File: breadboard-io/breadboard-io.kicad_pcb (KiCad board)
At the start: 2 copper layers, 33 x 19.1 mm, 25 parts, among them J1 Conn_01x10_Male, Q1 DMN3300U, Q2 DMN3300U, Q3 DMN3300U, Q4 DMN3300U, SW1 SW0, SW2 SW0, SW3 SW0, SW4 SW0

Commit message: Committing and ordering Rev-1
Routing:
- net GND: track 1.47 -> 0.00 mm
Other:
- board text added: "rev-1"

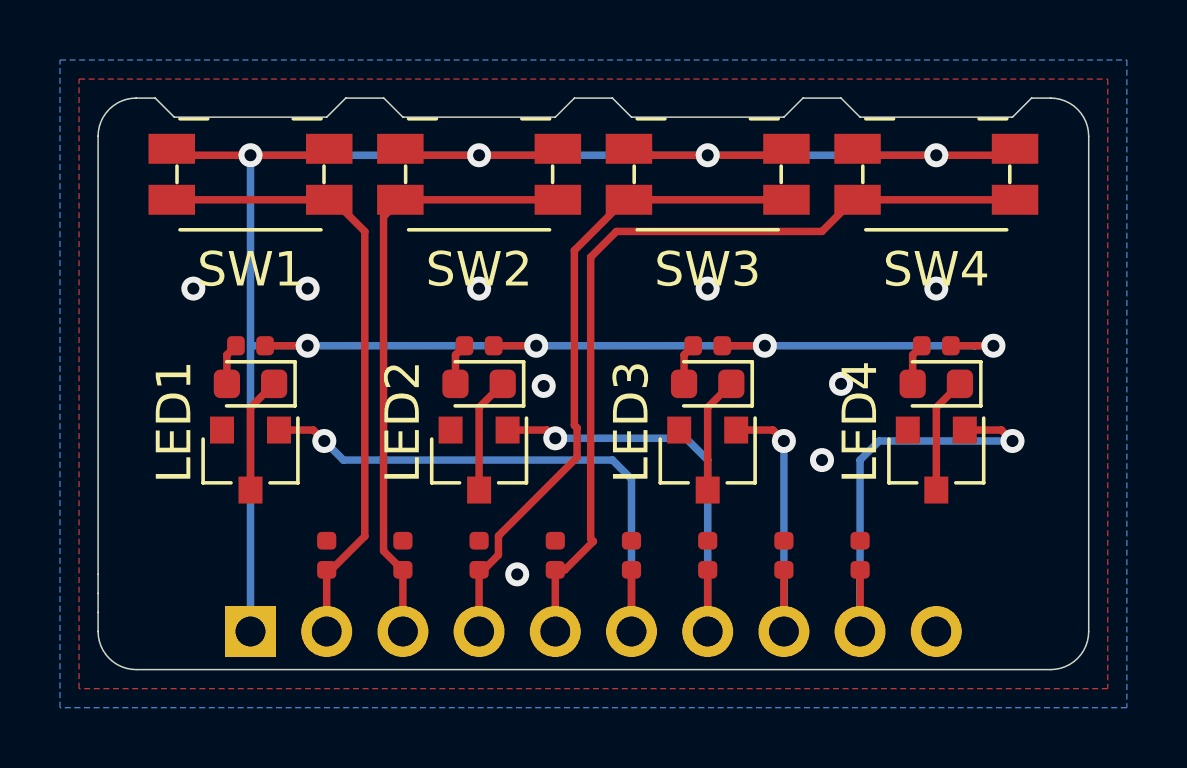
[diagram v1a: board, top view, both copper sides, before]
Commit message: Update models and add screenshot
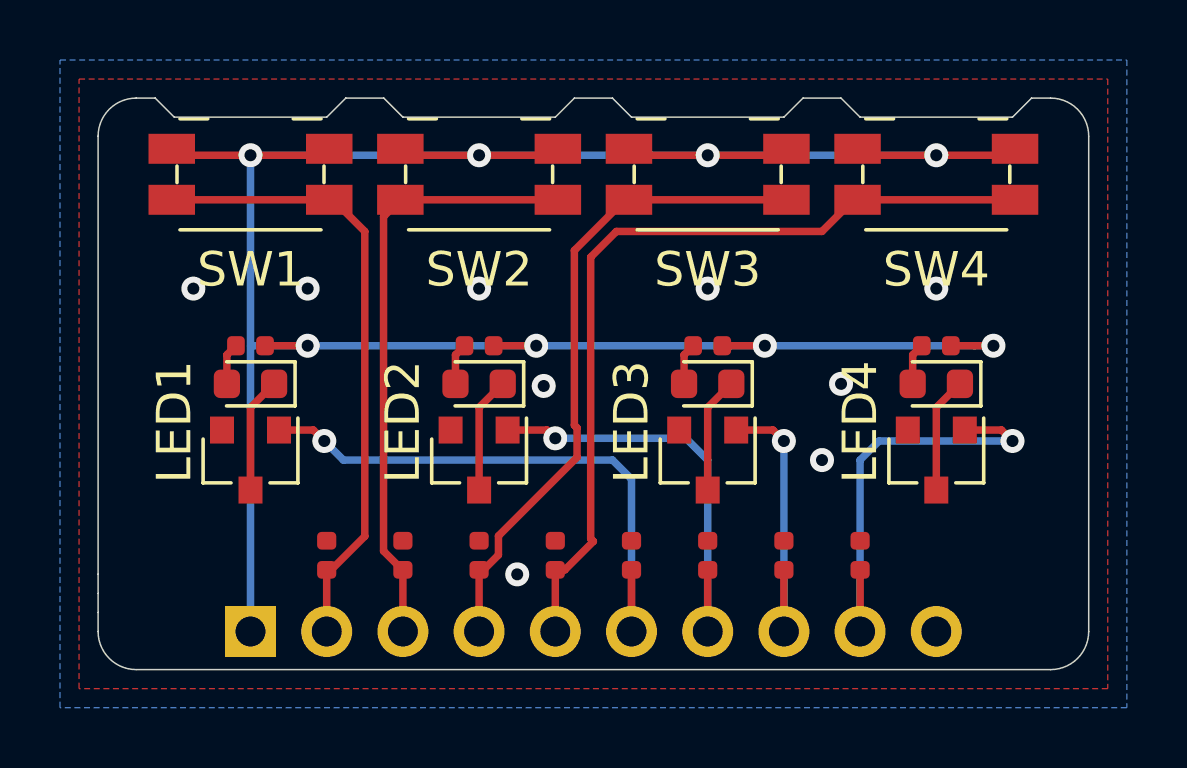
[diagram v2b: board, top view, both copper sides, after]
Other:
- outline, holes or cut-outs redrawn
- net class Default removed

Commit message: Added padding resistors to the push-button output lines and cleaned up the README
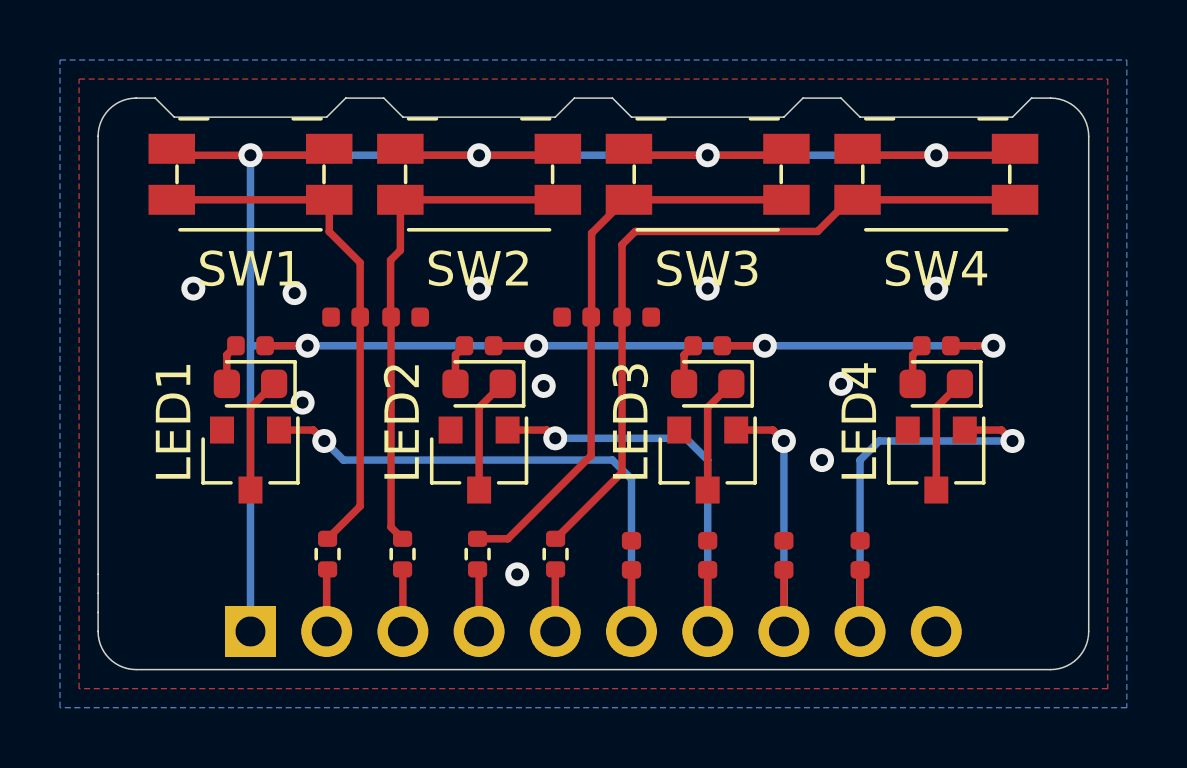
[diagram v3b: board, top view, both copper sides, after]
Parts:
- added G***: LOGO, breadboard-io:gld-logo, B.Cu at (148.0, 107.6)
- added R13: 1k, Resistor_SMD:R_0402_1005Metric, F.Cu at (128.3, 116.8)
- added R14: 1k, Resistor_SMD:R_0402_1005Metric, F.Cu at (130.8, 116.8)
- added R15: 1k, Resistor_SMD:R_0402_1005Metric, F.Cu at (133.3, 116.8)
- added R16: 1k, Resistor_SMD:R_0402_1005Metric, F.Cu at (135.9, 116.8)
- moved R3 8.58 mm to (136.6, 108.9), turned to 180 degrees
- moved R4 8.39 mm to (138.6, 108.9), turned to 0 degrees
- moved R1 7.96 mm to (128.9, 108.9), turned to 180 degrees
- moved R2 7.94 mm to (130.9, 108.9), turned to 0 degrees
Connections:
- R1 pad 1: SW0 -> Net-(SW1-Pad2)
- R2 pad 1: SW1 -> Net-(R2-Pad1)
- R3 pad 1: SW2 -> Net-(R3-Pad1)
- R4 pad 1: SW3 -> Net-(SW4-Pad2)
- SW1 pad 2: SW0 -> Net-(SW1-Pad2)
- SW2 pad 2: SW1 -> Net-(R2-Pad1)
- SW3 pad 2: SW2 -> Net-(R3-Pad1)
- SW4 pad 2: SW3 -> Net-(SW4-Pad2)
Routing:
- net SW3: track 28.2 -> 2.07 mm
- net Net-(SW4-Pad2): track 0.00 -> 24.4 mm
- net SW2: track 21.9 -> 2.09 mm
- net Net-(R3-Pad1): track 0.00 -> 19.3 mm
- net SW0: track 20.8 -> 2.08 mm
- net SW1: track 20.1 -> 2.07 mm
- net Net-(SW1-Pad2): track 0.00 -> 17.4 mm
- net Net-(R2-Pad1): track 0.00 -> 16.9 mm
- net GND: vias 9 -> 10
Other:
- board text added: "breadboard-io rev B"
- board text removed: "active-high"
- board text removed: "breadboard-io"
- board text removed: "github.com/stephendpmurphy CC-BY-SA"
- board text removed: "rev-1"

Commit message: Testing schematic generation with hierachial sheets
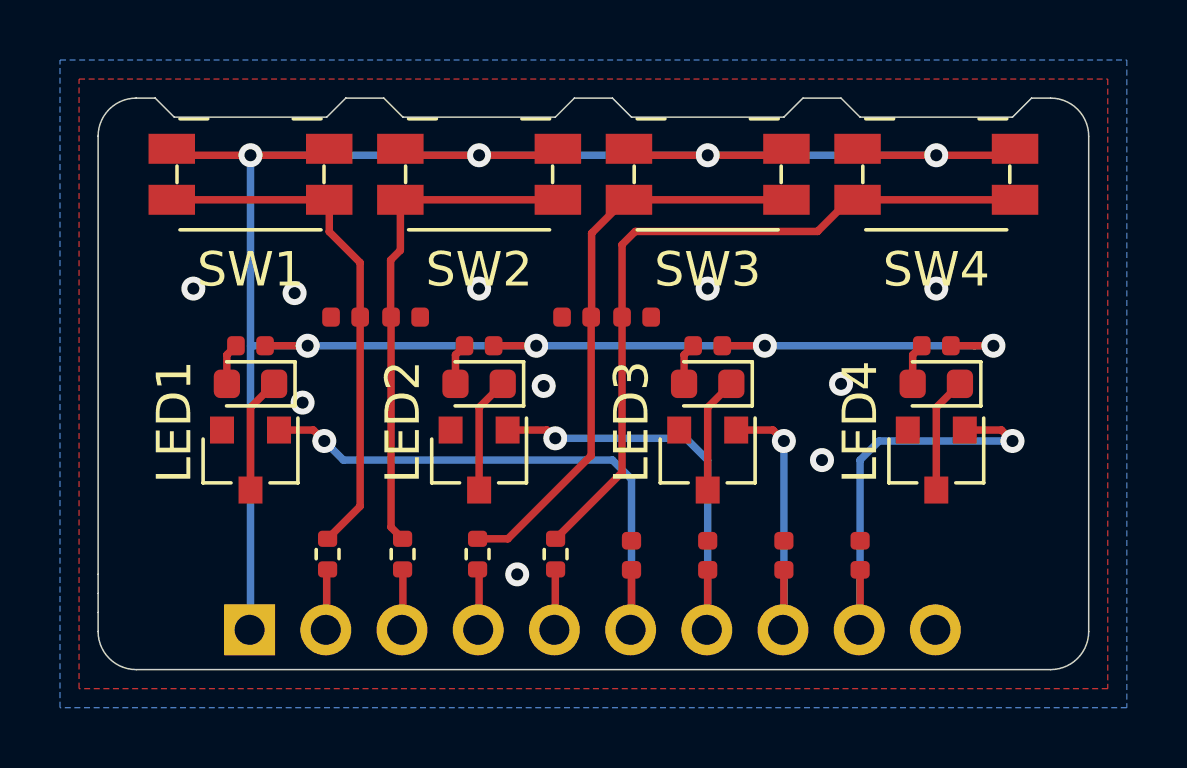
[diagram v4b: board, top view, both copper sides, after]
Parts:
- moved J1 0.06 mm to (125.7, 119.3)
